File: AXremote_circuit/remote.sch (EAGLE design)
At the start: 22 parts, among them Q2 32kHz, U1 AX8052F143HS

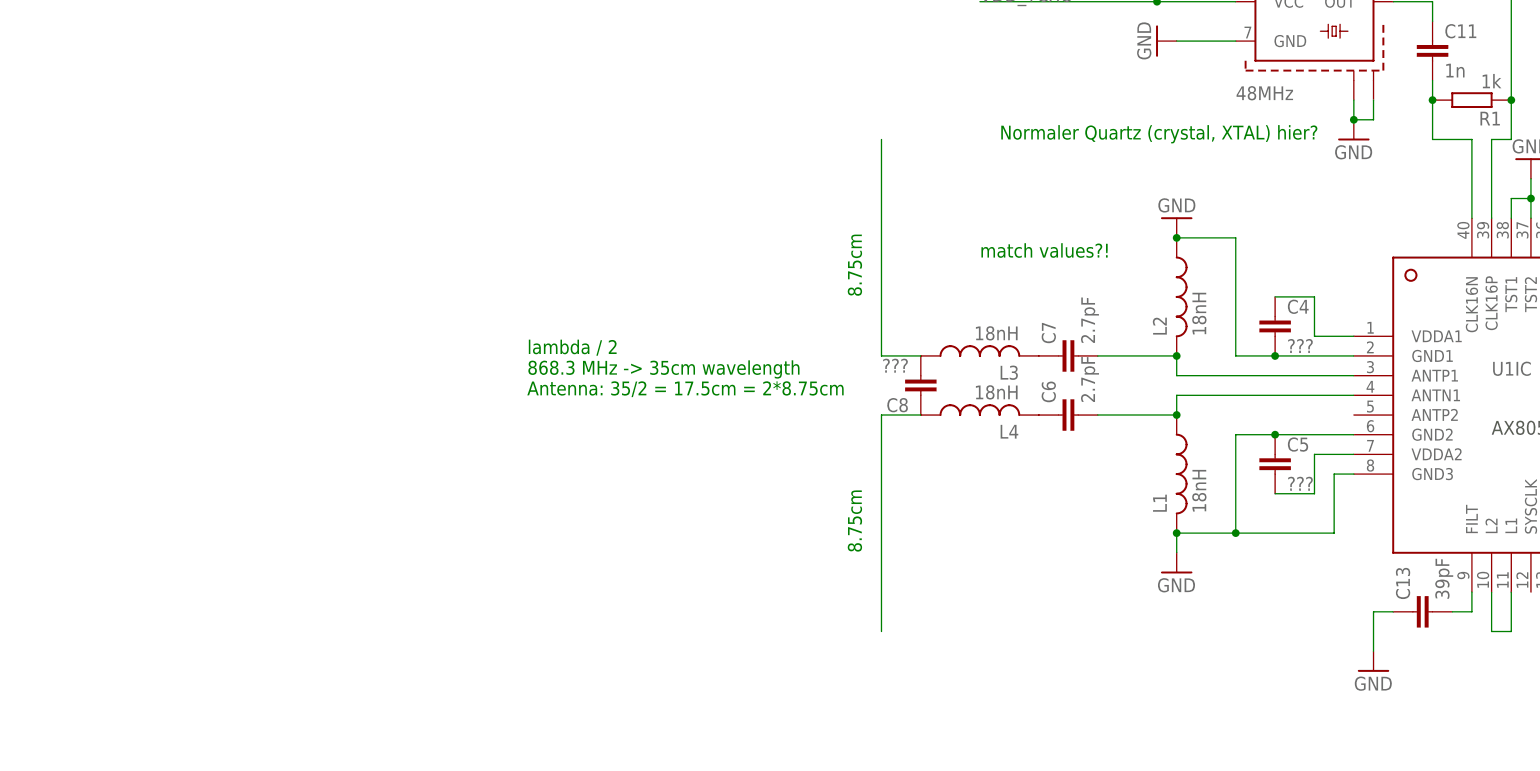
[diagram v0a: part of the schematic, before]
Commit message: Change schematics to single-ended.
Warning: Commit contains temporary files.
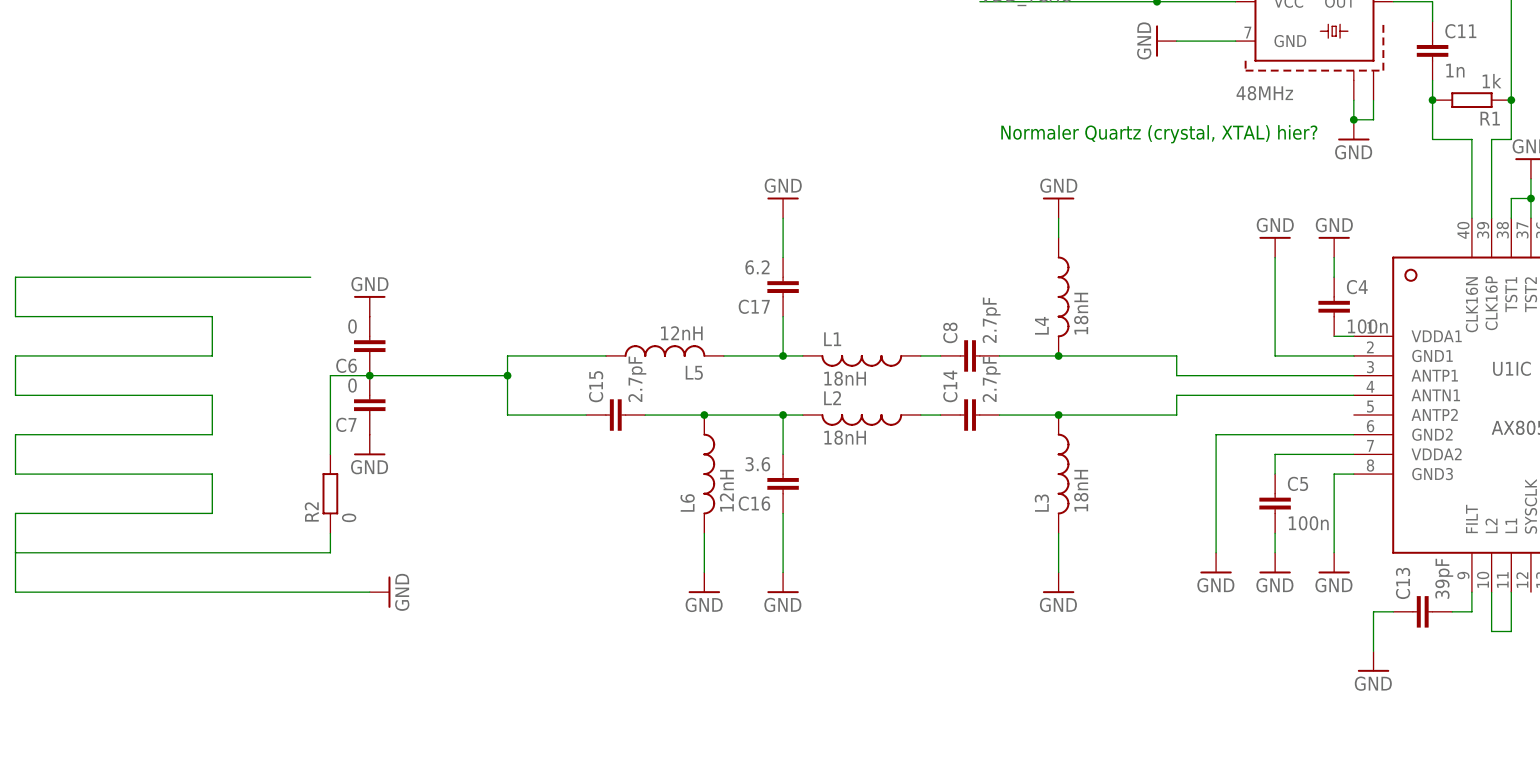
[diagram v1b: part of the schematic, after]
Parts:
- added C14, C15: 2.7pF, resistor:C-EUC0805
- added C16: 3.6, resistor:C-EUC0805
- added C17: 6.2, resistor:C-EUC0805
- added L5, L6: 12nH, resistor:L-USL4035M
- added R2: 0, resistor:R-EU_R0603
- C4, C5: value ??? -> 100n
- C6, C7: value 2.7pF -> 0
- C8: value ??? -> 2.7pF
- L1, L2, L3, L4: device resistor:L-USL3230M -> resistor:L-USL4035M
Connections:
- removed net N$14: C6.1, L4.2
- removed net N$15: C8.1, L4.1
- new net N$10: C14.1, L2.1
- new net N$11: C15.1, C6.1, C7.2, L5.1, R2.2
- new net N$8: C14.2, L3.1, U1IC.ANTN1
- net GND: now also C16.1, C17.2, C4.1, C5.2, C6.2, C7.1, L3.2, L4.1, L6.2, R2.1; no longer C4.2, C5.1, L1.2, L2.1
- net N$12: now also C17.1, L1.2, L5.2; no longer C7.1, L3.2
- net N$13: now also C15.2, C16.2, L2.2, L6.1; no longer C8.2, L3.1
- net N$3: now also C4.2, U1IC.VDDA1; no longer C5.2, U1IC.VDDA2
- net N$6: now also C5.1, U1IC.VDDA2; no longer C6.2, L1.1, U1IC.ANTN1
- net N$7: now also C8.2, L4.2; no longer C7.2, L2.2
- net N$9: now also C8.1, L1.1; no longer C4.1, U1IC.VDDA1
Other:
- note removed: "8.75cm"
- note removed: "lambda / 2 868.3 MHz -> 35cm wavelength Antenna: 35/2 = 17.5cm = 2*8.75cm"
- note removed: "match values?!"
- moved on the sheet: C4, C5, C6, C7, C8, L1, L2, L3, L4

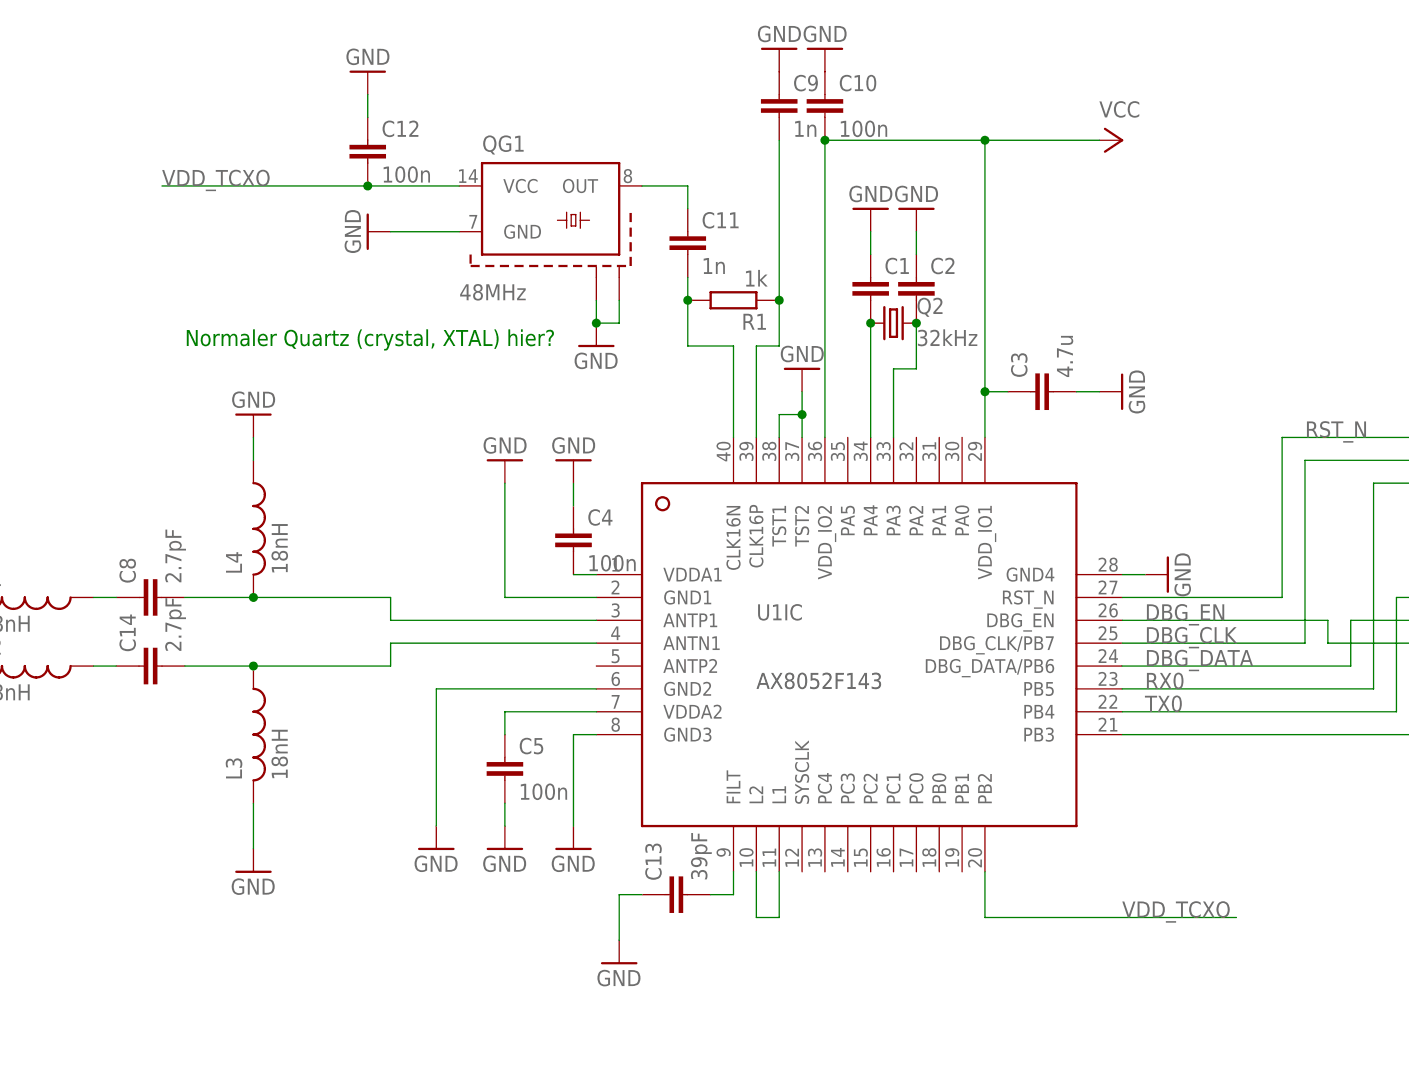
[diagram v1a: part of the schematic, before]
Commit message: Simplified schematics (only one crystal).
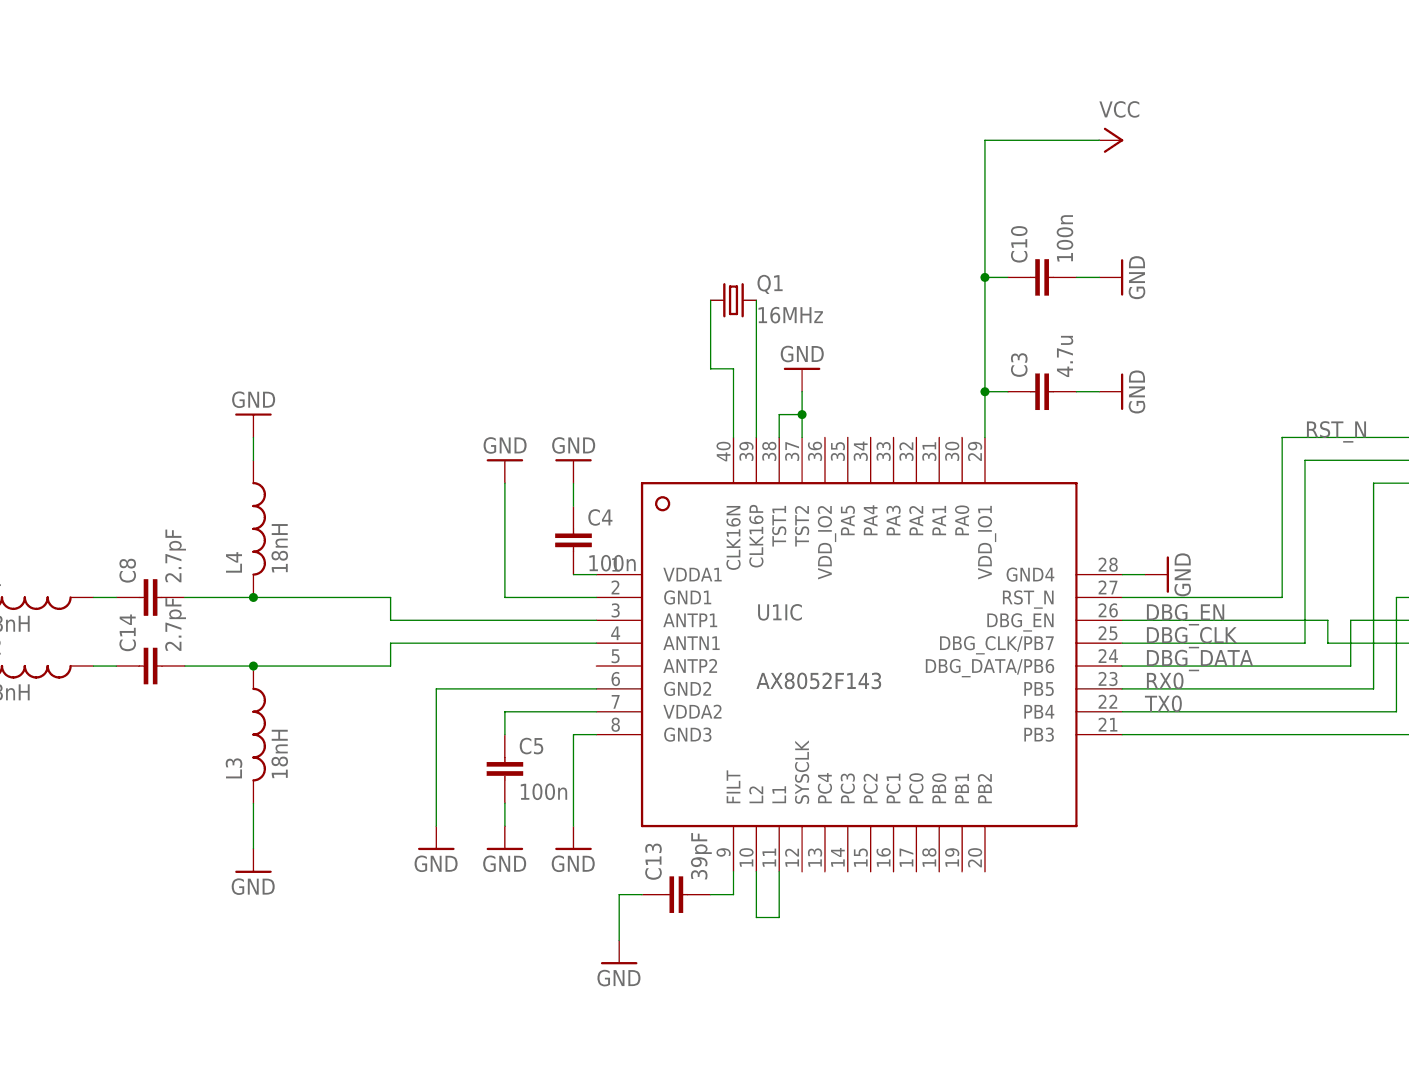
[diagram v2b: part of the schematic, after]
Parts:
- removed C1, C2: (no value), resistor:C-EUC0805
- removed C11, C9: 1n, resistor:C-EUC0805
- removed C12: 100n, resistor:C-EUC0805
- removed Q2: 32kHz, crystal:CRYSTALSM49
- removed QG1: 48MHz, crystal:TC47H
- removed R1: 1k, resistor:R-EU_R0603
- added Q1: 16MHz, crystal:CRYSTALSM49
- C10, C4, C5: device resistor:C-EUC0805 -> resistor:C-EUC1206
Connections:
- removed net N$20: C9.2, R1.1, U1IC.CLK16P
- removed net N$21: C11.2, R1.2, U1IC.CLK16N
- removed net N$22: C11.1, QG1.OUT
- removed net N$4: C1.2, Q2.1, U1IC.PA4
- removed net N$5: C2.2, Q2.2, U1IC.PA3
- removed net VDD_TCXO: C12.2, QG1.VCC, U1IC.PB2
- new net N$14: Q1.2, U1IC.CLK16P
- new net N$15: Q1.1, U1IC.CLK16N
- net GND: now also C10.2; no longer C1.1, C10.1, C12.1, C2.1, C9.1, QG1.GND, QG1.S1, QG1.S2
- net VCC: now also C10.1; no longer C10.2, U1IC.VDD_IO2
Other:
- note removed: "Normaler Quartz (crystal, XTAL) hier?"
- moved on the sheet: C10

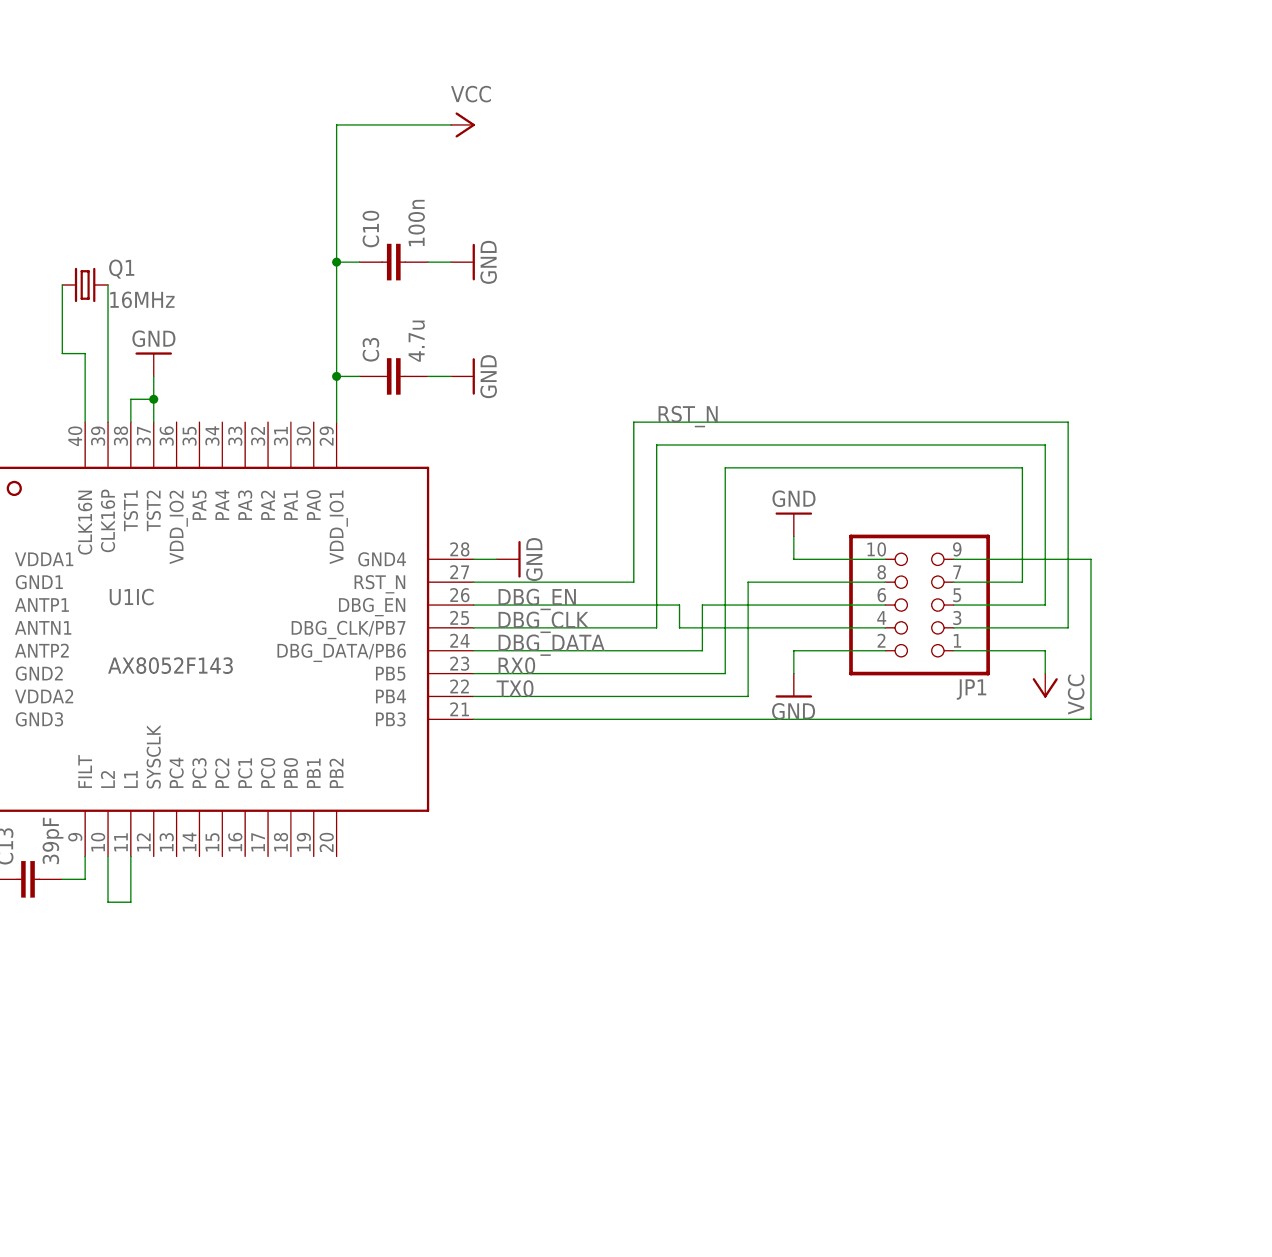
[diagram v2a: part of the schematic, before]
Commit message: Layouted board with antenna.
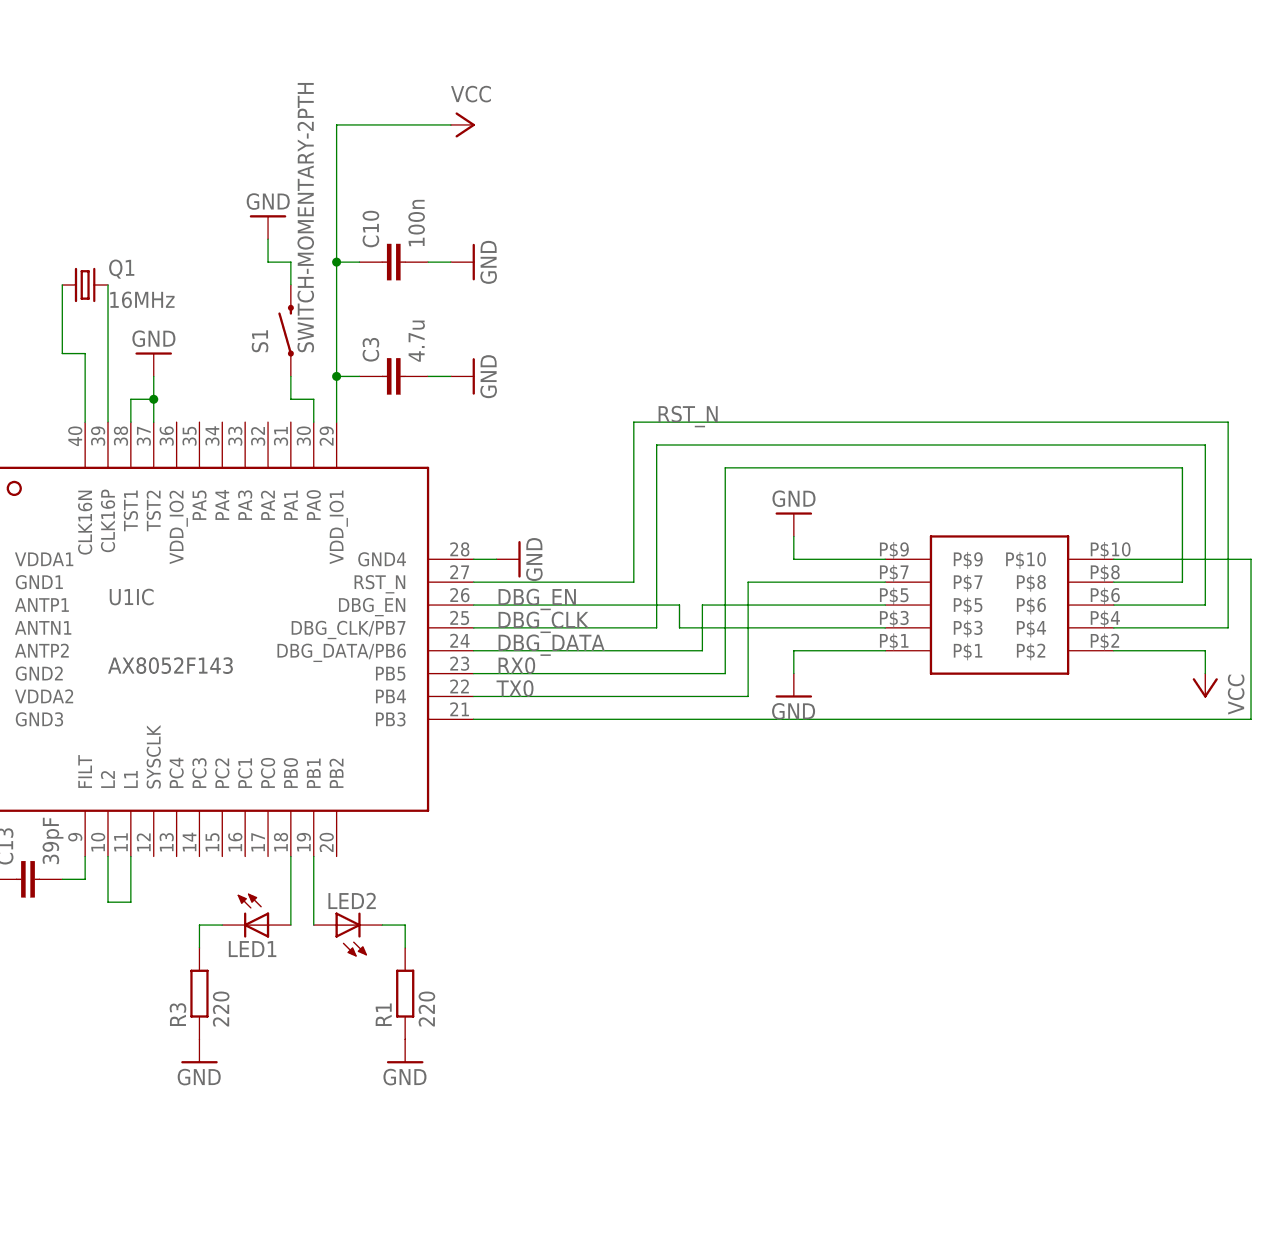
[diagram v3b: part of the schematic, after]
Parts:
- removed JP1: (no value), pinhead:PINHD-2X5
- added LED1, LED2: (no value), led:LEDCHIPLED_0805
- added R1, R3: 220, resistor:R-EU_R0603
- added S1: SWITCH-MOMENTARY-2PTH, SparkFun-Electromechanical:SWITCH-MOMENTARY-2PTH
- added U$1: PINHEADER5X2, sam:PINHEADER5X2
- L1, L2, L3, L4, L5, L6: device resistor:L-USL4035M -> resistor:L-US0603
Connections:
- new net N$16: LED2.A, U1IC.PB1
- new net N$17: LED1.A, U1IC.PB0
- new net N$19: S1.1, U1IC.PA0
- new net N$4: LED1.C, R3.2
- new net N$5: LED2.C, R1.2
- net DBG_CLK: now also U$1.P$6; no longer JP1.5
- net DBG_DATA: now also U$1.P$5; no longer JP1.6
- net DBG_EN: now also U$1.P$3; no longer JP1.4
- net GND: now also R1.1, R3.1, S1.2, U$1.P$1, U$1.P$9; no longer JP1.10, JP1.2
- net N$18: now also U$1.P$10; no longer JP1.9
- net RST_N: now also U$1.P$4; no longer JP1.3
- net RX0: now also U$1.P$8; no longer JP1.7
- net TX0: now also U$1.P$7; no longer JP1.8
- net VCC: now also U$1.P$2; no longer JP1.1

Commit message: Moved antenna components closer to chip, better ground connection[s].
According to Thomas' tips.
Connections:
- removed net N$17: LED1.A, U1IC.PB0
- new net N$20: C15.1, C7.2, L5.1, R2.2
- net GND: now also C6.1
- net N$11: now also LED1.A, U1IC.PA1; no longer C15.1, C6.1, C7.2, L5.1, R2.2
- net N$16: now also U1IC.PA2; no longer U1IC.PB1
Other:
- moved on the sheet: C6, LED1, LED2, R1, R3, S1

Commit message: Fix progconnector in schematic. Add TODOs.
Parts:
- removed LED1, LED2: (no value), led:LEDCHIPLED_0805
- removed R1, R3: 220, resistor:R-EU_R0603
- removed S1: SWITCH-MOMENTARY-2PTH, SparkFun-Electromechanical:SWITCH-MOMENTARY-2PTH
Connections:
- removed net N$11: LED1.A, U1IC.PA1
- removed net N$18: U$1.P$10, U1IC.PB3
- removed net N$19: S1.1, U1IC.PA0
- removed net N$4: LED2.C, R1.2
- removed net RST_N: U$1.P$4, U1IC.RST_N
- new net BATTMEASURE: U1IC.PA0
- net DBG_CLK: now also U$1.P$5; no longer U$1.P$6
- net DBG_DATA: now also U$1.P$6; no longer U$1.P$5
- net DBG_EN: now also U$1.P$4; no longer U$1.P$3
- net GND: now also U$1.P$10, U$1.P$2; no longer R1.1, R3.1, S1.2, U$1.P$1, U$1.P$9
- net N$16: now also U$1.P$9, U1IC.PB3; no longer LED2.A, U1IC.PA2
- net N$5: now also U$1.P$3, U1IC.RST_N; no longer LED1.C, R3.2
- net RX0: now also U$1.P$7; no longer U$1.P$8
- net TX0: now also U$1.P$8; no longer U$1.P$7
- net VCC: now also U$1.P$1, U1IC.VDD_IO2; no longer U$1.P$2
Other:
- note added: "todo: - buttons (matrix, shift reg, ..?) - battery measurement - low power led - status (tx)/debug led - battery, ev. regulator - on/off switch"
